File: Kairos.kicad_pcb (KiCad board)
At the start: 2 copper layers, 285 x 94.6 mm, 136 parts, among them Q1 NSS40301MZ4T1G, SW1 SW_RST1, U1 ATMEGA32U2-AU, Y1 Crystal_GND24

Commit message: Prepare for switch location testing
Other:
- board text added: "107.15625"
- board text removed: "HHKB Layout"
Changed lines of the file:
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@@
     (effects (font (size 1.5 1.5) (thickness 0.3)))
   )
-  (gr_text "HHKB\nLayout" (at 255.5875 149.225) (layer Dwgs.User)
+  (gr_text 107.15625 (at 237.33125 150.8125) (layer Dwgs.User)
     (effects (font (size 1.5 1.5) (thickness 0.3)))
   )

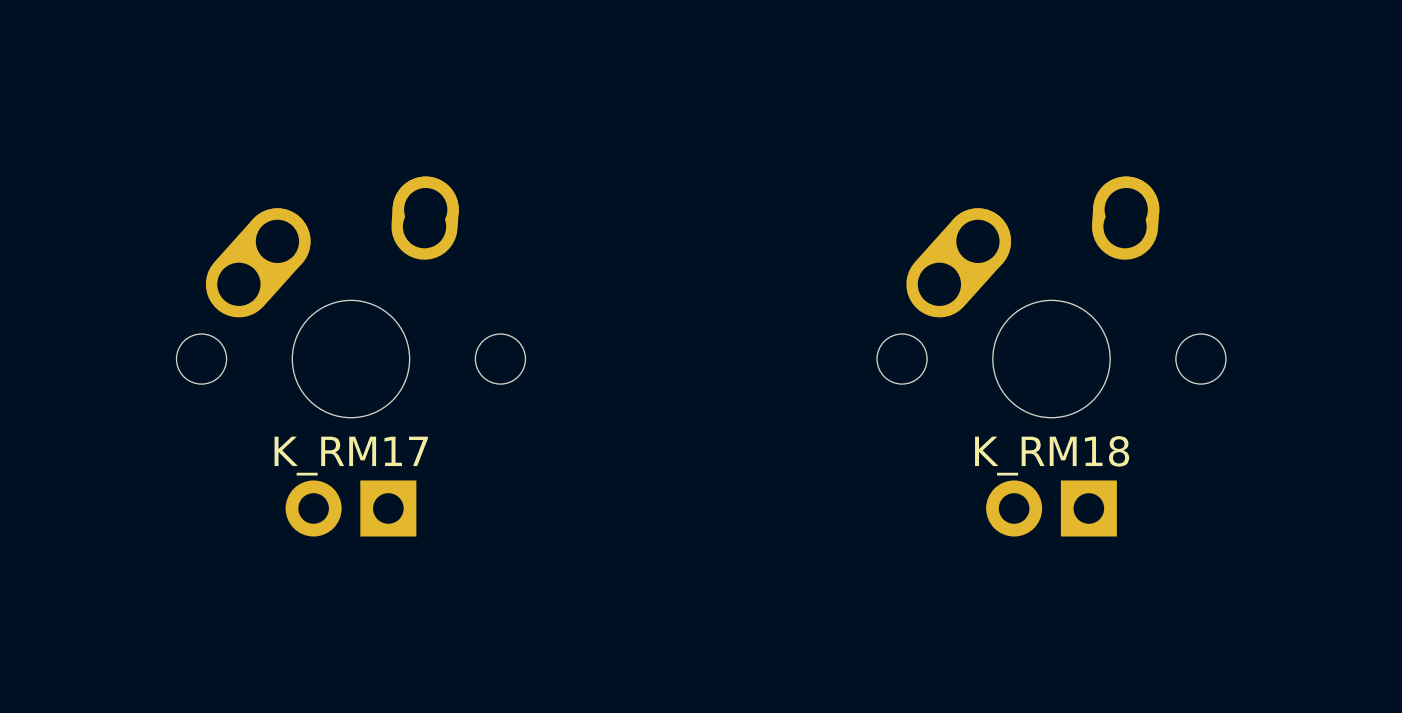
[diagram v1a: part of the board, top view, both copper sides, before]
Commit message: Remove RM17, RM18
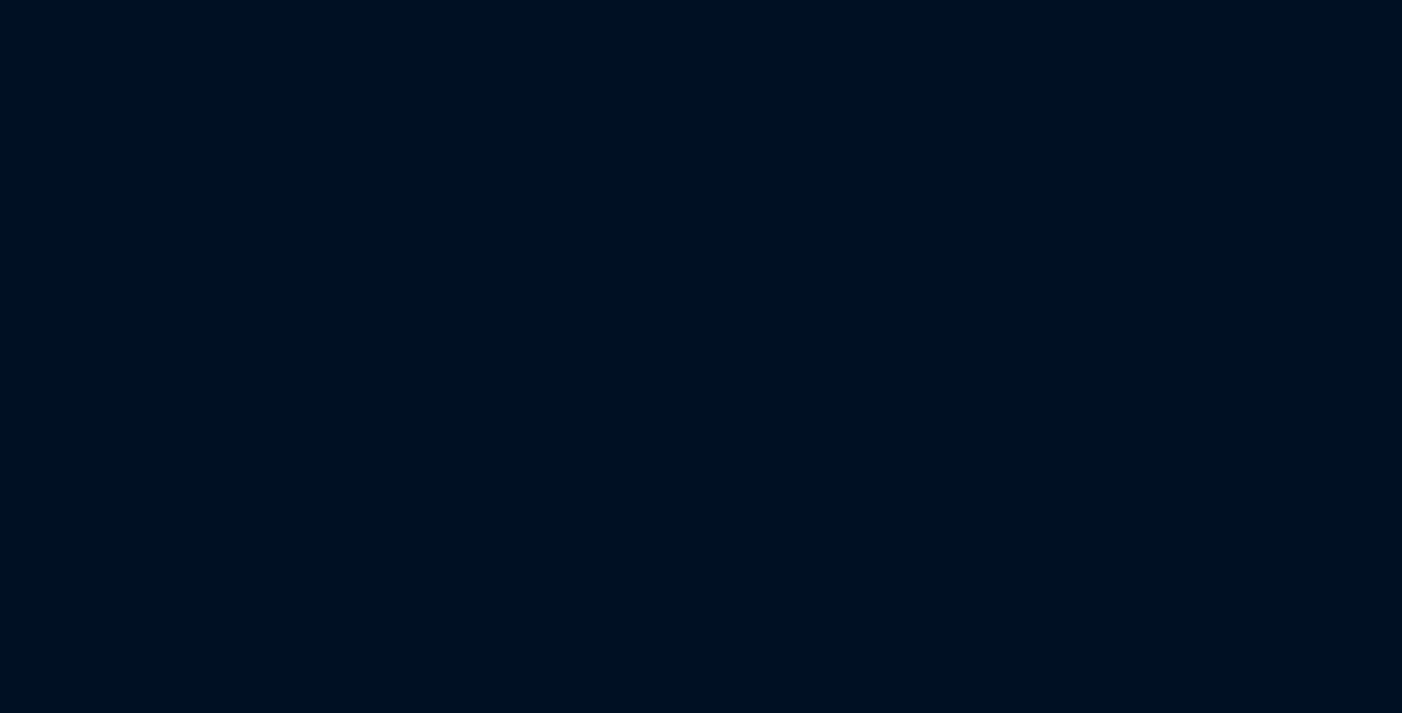
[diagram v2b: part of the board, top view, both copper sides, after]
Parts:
- removed K_RM17: MX-1.5U, MX_Alps_Hybrid:MX-1.5U
- removed K_RM18: MX-1U, MX_Alps_Hybrid:MX-1U
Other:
- board text added: "Split 6 Combined with 2.75 from Var2, Shares 2.75 from Var1 for 2.25"
- board text removed: "Orphaned 1U (Perhaps a 2.25U existed to its left before)"
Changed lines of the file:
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@@
 (kicad_pcb (version 4) (host pcbnew 4.0.6)
   (general
-    (links 585)
-    (no_connects 315)
+    (links 573)
+    (no_connects 307)
     (area 0 0 0 0)
     (thickness 1.6)
@@
     (tracks 278)
     (zones 0)
-    (modules 136)
+    (modules 134)
     (nets 189)
   )
@@
   (net 186 "Net-(DRS3-Pad2)")
   (net 187 "Net-(K_SP10-Pad3)")
-  (net 188 "Net-(K_RM18-Pad3)")
+  (net 188 "Net-(K_RM8-Pad3)")
   (net_class Default "This is the default net class."
     (clearance 0.2)
@@
     (add_net "Net-(K_RM13-Pad3)")
     (add_net "Net-(K_RM14-Pad3)")
-    (add_net "Net-(K_RM18-Pad3)")
+    (add_net "Net-(K_RM8-Pad3)")
     (add_net "Net-(K_RS1-Pad3)")
     (add_net "Net-(K_RS4-Pad3)")
@@
   )
   (module MX_Alps_Hybrid:MX-1.5U (layer F.Cu)
-    (at 209.55 247.65)
-    (fp_text reference K_RM17 (at 0 3.175) (layer F.SilkS)
-      (effects (font (size 1 1) (thickness 0.15)))
-    )
-    (fp_text value MX-1.5U (at 0 -7.9375) (layer Dwgs.User)
-      (effects (font (size 1 1) (thickness 0.15)))
-    )
-    (fp_line (start 5 -7) (end 7 -7) (layer Dwgs.User) (width 0.15))
-    (fp_line (start 7 -7) (end 7 -5) (layer Dwgs.User) (width 0.15))
-    (fp_line (start 5 7) (end 7 7) (layer Dwgs.User) (width 0.15))
-    (fp_line (start 7 7) (end 7 5) (layer Dwgs.User) (width 0.15))
-    (fp_line (start -7 5) (end -7 7) (layer Dwgs.User) (width 0.15))
-    (fp_line (start -7 7) (end -5 7) (layer Dwgs.User) (width 0.15))
-    (fp_line (start -5 -7) (end -7 -7) (layer Dwgs.User) (width 0.15))
-    (fp_line (start -7 -7) (end -7 -5) (layer Dwgs.User) (width 0.15))
-    (fp_line (start -14.2875 -9.525) (end 14.2875 -9.525) (layer Dwgs.User) (width 0.15))
-    (fp_line (start 14.2875 -9.525) (end 14.2875 9.525) (layer Dwgs.User) (width 0.15))
-    (fp_line (start -14.2875 9.525) (end 14.2875 9.525) (layer Dwgs.User) (width 0.15))
-    (fp_line (start -14.2875 9.525) (end -14.2875 -9.525) (layer Dwgs.User) (width 0.15))
-    (pad 2 thru_hole oval (at 2.5 -4.5 86.0548) (size 2.831378 2.25) (drill 1.47 (offset 0.290689 0)) (layers *.Cu *.Mask)
-      (net 179 "Net-(DRM1-Pad2)"))
-    (pad 2 thru_hole circle (at 2.54 -5.08) (size 2.25 2.25) (drill 1.47) (layers *.Cu *.Mask)
-      (net 179 "Net-(DRM1-Pad2)"))
-    (pad 1 thru_hole oval (at -3.81 -2.54 48.09963212) (size 4.211556 2.25) (drill 1.47 (offset 0.980778 0)) (layers *.Cu *.Mask)
-      (net 107 COL5))
-    (pad "" np_thru_hole circle (at 0 0) (size 3.9878 3.9878) (drill 3.9878) (layers *.Cu *.Mask))
-    (pad 1 thru_hole circle (at -2.5 -4) (size 2.25 2.25) (drill 1.47) (layers *.Cu *.Mask)
-      (net 107 COL5))
-    (pad 3 thru_hole circle (at -1.27 5.08) (size 1.905 1.905) (drill 1.04) (layers *.Cu *.Mask)
-      (net 45 "Net-(K_RM1-Pad3)"))
-    (pad 4 thru_hole rect (at 1.27 5.08) (size 1.905 1.905) (drill 1.04) (layers *.Cu *.Mask)
-      (net 2 LEDGND))
-    (pad "" np_thru_hole circle (at -5.08 0 48.0996) (size 1.7018 1.7018) (drill 1.7018) (layers *.Cu *.Mask))
-    (pad "" np_thru_hole circle (at 5.08 0 48.0996) (size 1.7018 1.7018) (drill 1.7018) (layers *.Cu *.Mask))
-  )
-  (module MX_Alps_Hybrid:MX-1.5U (layer F.Cu)
     (at 223.8375 285.75)
     (fp_text reference K_RM13 (at 0 3.175) (layer F.SilkS)
@@
       (net 120 COL6))
     (pad 3 thru_hole circle (at -1.27 5.08) (size 1.905 1.905) (drill 1.04) (layers *.Cu *.Mask)
-      (net 188 "Net-(K_RM18-Pad3)"))
+      (net 188 "Net-(K_RM8-Pad3)"))
     (pad 4 thru_hole rect (at 1.27 5.08) (size 1.905 1.905) (drill 1.04) (layers *.Cu *.Mask)
       (net 2 LEDGND))
@@
     (pad "" np_thru_hole circle (at 5.08 0 48.0996) (size 1.7018 1.7018) (drill 1.7018) (layers *.Cu *.Mask))
   )
-  (module MX_Alps_Hybrid:MX-1U (layer F.Cu)
-    (at 233.3625 247.65)
-    (fp_text reference K_RM18 (at 0 3.175) (layer F.SilkS)
-      (effects (font (size 1 1) (thickness 0.15)))
-    )
-    (fp_text value MX-1U (at 0 -7.9375) (layer Dwgs.User)
-      (effects (font (size 1 1) (thickness 0.15)))
-    )
-    (fp_line (start 5 -7) (end 7 -7) (layer Dwgs.User) (width 0.15))
-    (fp_line (start 7 -7) (end 7 -5) (layer Dwgs.User) (width 0.15))
-    (fp_line (start 5 7) (end 7 7) (layer Dwgs.User) (width 0.15))
-    (fp_line (start 7 7) (end 7 5) (layer Dwgs.User) (width 0.15))
-    (fp_line (start -7 5) (end -7 7) (layer Dwgs.User) (width 0.15))
-    (fp_line (start -7 7) (end -5 7) (layer Dwgs.User) (width 0.15))
-    (fp_line (start -5 -7) (end -7 -7) (layer Dwgs.User) (width 0.15))
-    (fp_line (start -7 -7) (end -7 -5) (layer Dwgs.User) (width 0.15))
-    (fp_line (start -9.525 -9.525) (end 9.525 -9.525) (layer Dwgs.User) (width 0.15))
-    (fp_line (start 9.525 -9.525) (end 9.525 9.525) (layer Dwgs.User) (width 0.15))
-    (fp_line (start 9.525 9.525) (end -9.525 9.525) (layer Dwgs.User) (width 0.15))
-    (fp_line (start -9.525 9.525) (end -9.525 -9.525) (layer Dwgs.User) (width 0.15))
-    (pad 2 thru_hole oval (at 2.5 -4.5 86.0548) (size 2.831378 2.25) (drill 1.47 (offset 0.290689 0)) (layers *.Cu *.Mask)
-      (net 182 "Net-(DRM3-Pad2)"))
-    (pad 2 thru_hole circle (at 2.54 -5.08) (size 2.25 2.25) (drill 1.47) (layers *.Cu *.Mask)
-      (net 182 "Net-(DRM3-Pad2)"))
-    (pad 1 thru_hole oval (at -3.81 -2.54 48.09963212) (size 4.211556 2.25) (drill 1.47 (offset 0.980778 0)) (layers *.Cu *.Mask)
-      (net 120 COL6))
-    (pad "" np_thru_hole circle (at 0 0) (size 3.9878 3.9878) (drill 3.9878) (layers *.Cu *.Mask))
-    (pad 1 thru_hole circle (at -2.5 -4) (size 2.25 2.25) (drill 1.47) (layers *.Cu *.Mask)
-      (net 120 COL6))
-    (pad 3 thru_hole circle (at -1.27 5.08) (size 1.905 1.905) (drill 1.04) (layers *.Cu *.Mask)
-      (net 188 "Net-(K_RM18-Pad3)"))
-    (pad 4 thru_hole rect (at 1.27 5.08) (size 1.905 1.905) (drill 1.04) (layers *.Cu *.Mask)
-      (net 2 LEDGND))
-    (pad "" np_thru_hole circle (at -5.08 0 48.0996) (size 1.7018 1.7018) (drill 1.7018) (layers *.Cu *.Mask))
-    (pad "" np_thru_hole circle (at 5.08 0 48.0996) (size 1.7018 1.7018) (drill 1.7018) (layers *.Cu *.Mask))
-  )
   (module MX_Alps_Hybrid:MX-2.25U (layer F.Cu)
     (at 26.19375 88.10625)
@@
     (effects (font (size 1.5 1.5) (thickness 0.3)))
   )
-  (gr_text "Orphaned 1U\n(Perhaps a 2.25U existed\nto its left before)\n" (at 160.3375 247.65) (layer Dwgs.User)
+  (gr_text "Split 6\nCombined with 2.75 from Var2,\nShares 2.75 from Var1 for 2.25\n" (at 164.30625 246.85625) (layer Dwgs.User)
     (effects (font (size 1.5 1.5) (thickness 0.3)))
   )
